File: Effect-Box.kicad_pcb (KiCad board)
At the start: 6 copper layers, 170 parts, among them J1 Conn_02x07_Odd_Even, J10 Power pins, J2 26642801RP2, J3 FH12A-10S-0.5SH55, J5 Conn_ARM_JTAG_SWD_20, J6 26642801RP2, J7 AudioJack3, J8 AudioJack3, J9 PJ-006A-SMT, SW0 SW_Push, SW1 SW_Push, SW2 SW_Push, SW3 SW_Push, SW4 SW_Push, SW5 SW_Push, SW6 SW_Push, U1 TPS54325, U10 LM7805SX_NOPB, U2 TPS54294, U3 XC7A100T-FTG256, U4 S25FL1, U5 SiT2024B, U6 AS6C1616, U7 EFM32GG942F1024, U8 INA1651IPW, U9 PCM3003E

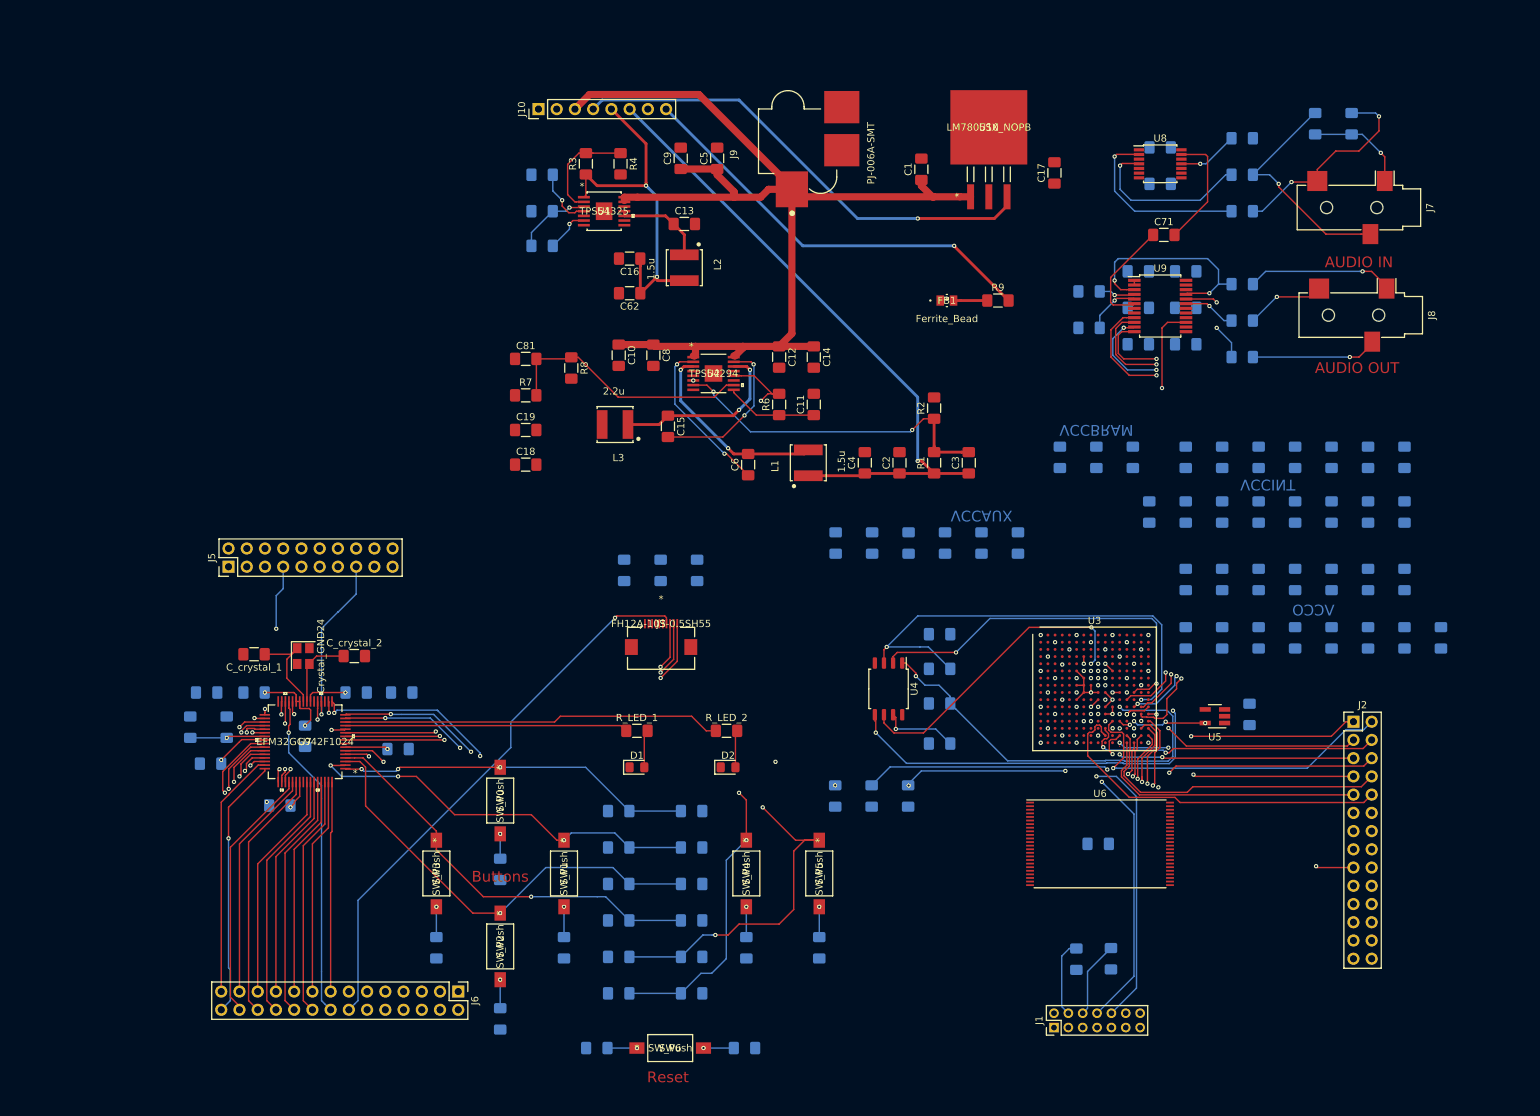
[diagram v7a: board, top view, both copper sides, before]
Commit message: Set up ground layer
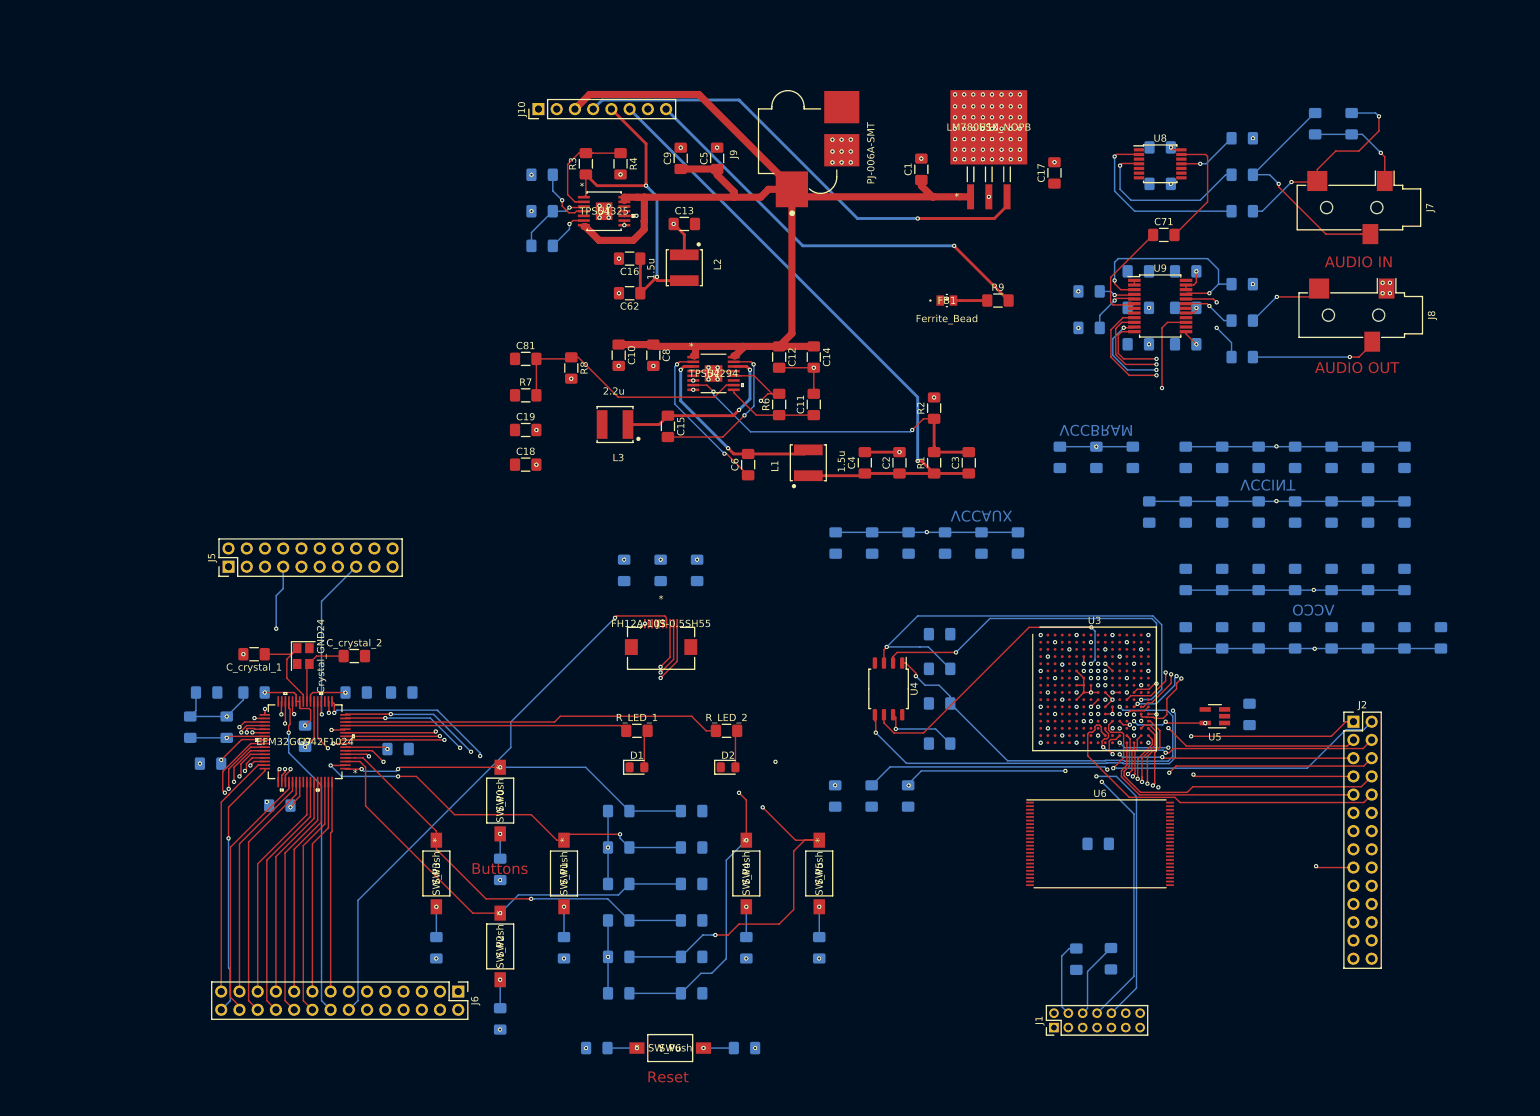
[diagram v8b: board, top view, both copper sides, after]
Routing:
- net GND: track 33.5 -> 252.8 mm, vias 36 -> 168
- net PWR_IN: track 153.7 -> 168.0 mm
- net Net-(C_btn_2-Pad1): track 62.2 -> 60.3 mm
- net Net-(C_reset1-Pad1): track 93.9 -> 95.3 mm
- net /FPGA/GPIO_3: track 138.7 -> 139.2 mm
- net Net-(C13-Pad1): vias 0 -> 2
- added copper zone on GND.Cu, net GND
